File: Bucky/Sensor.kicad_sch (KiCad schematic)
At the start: 4 parts, among them IC2001 INA239AQDGSRQ1

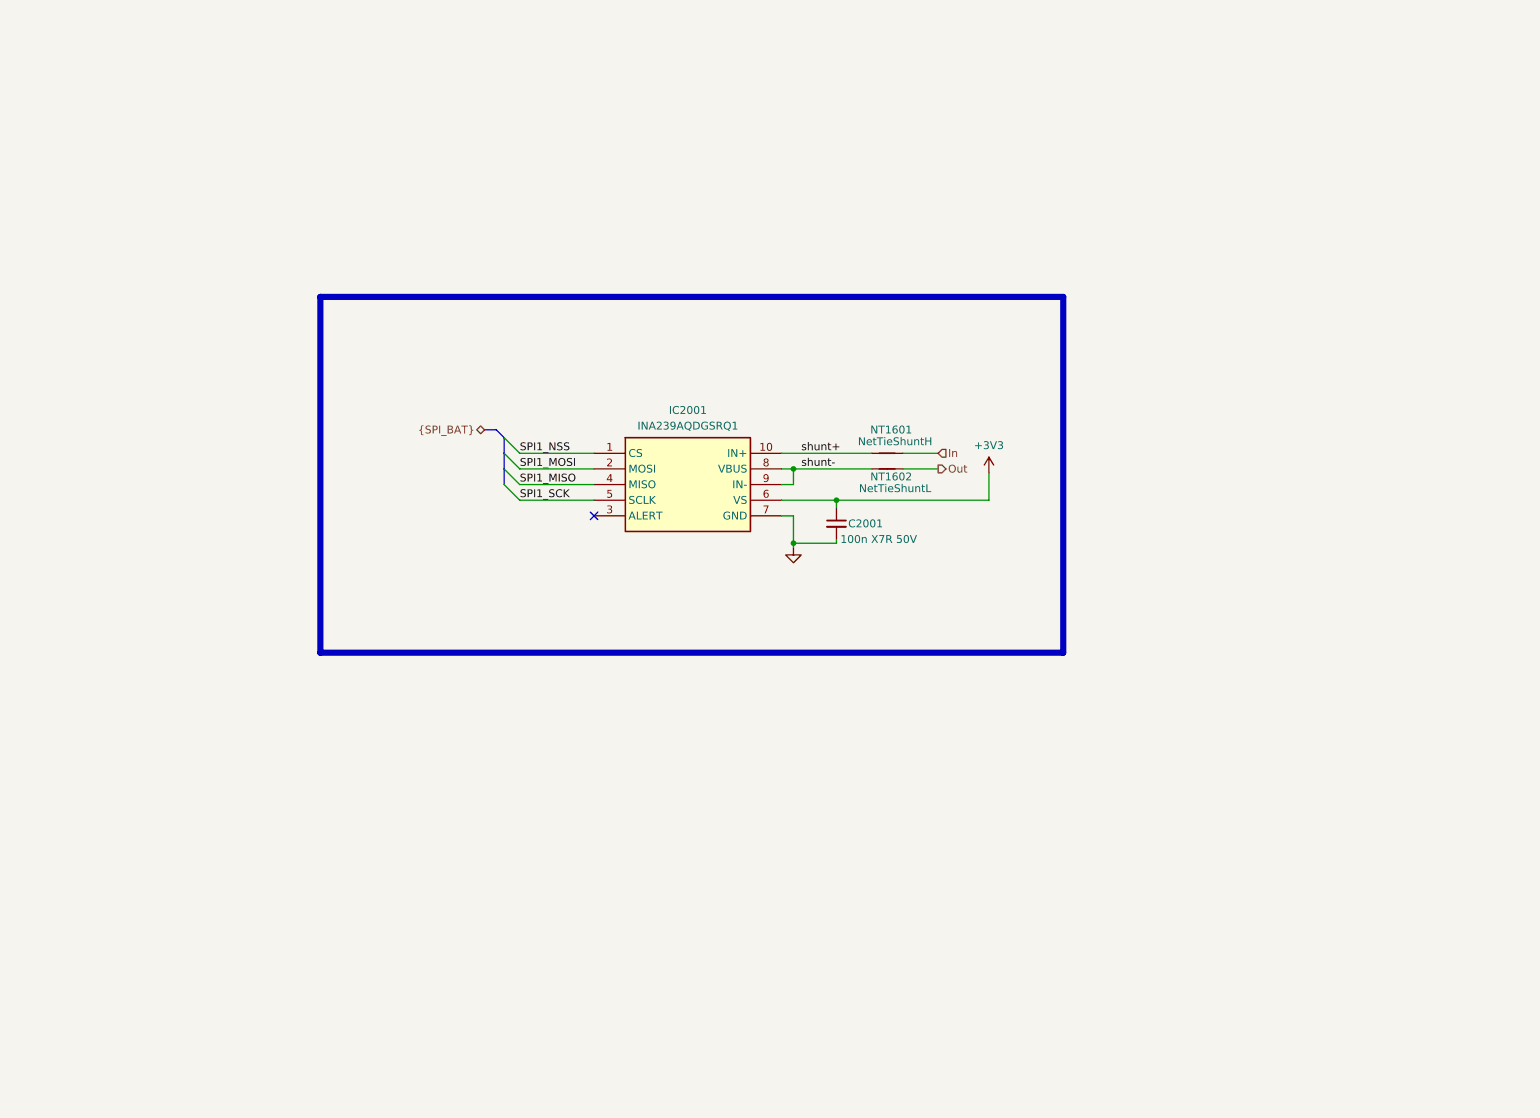
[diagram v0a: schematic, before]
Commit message: adapted schematics and added more protection from GEODE (Reverse Current)
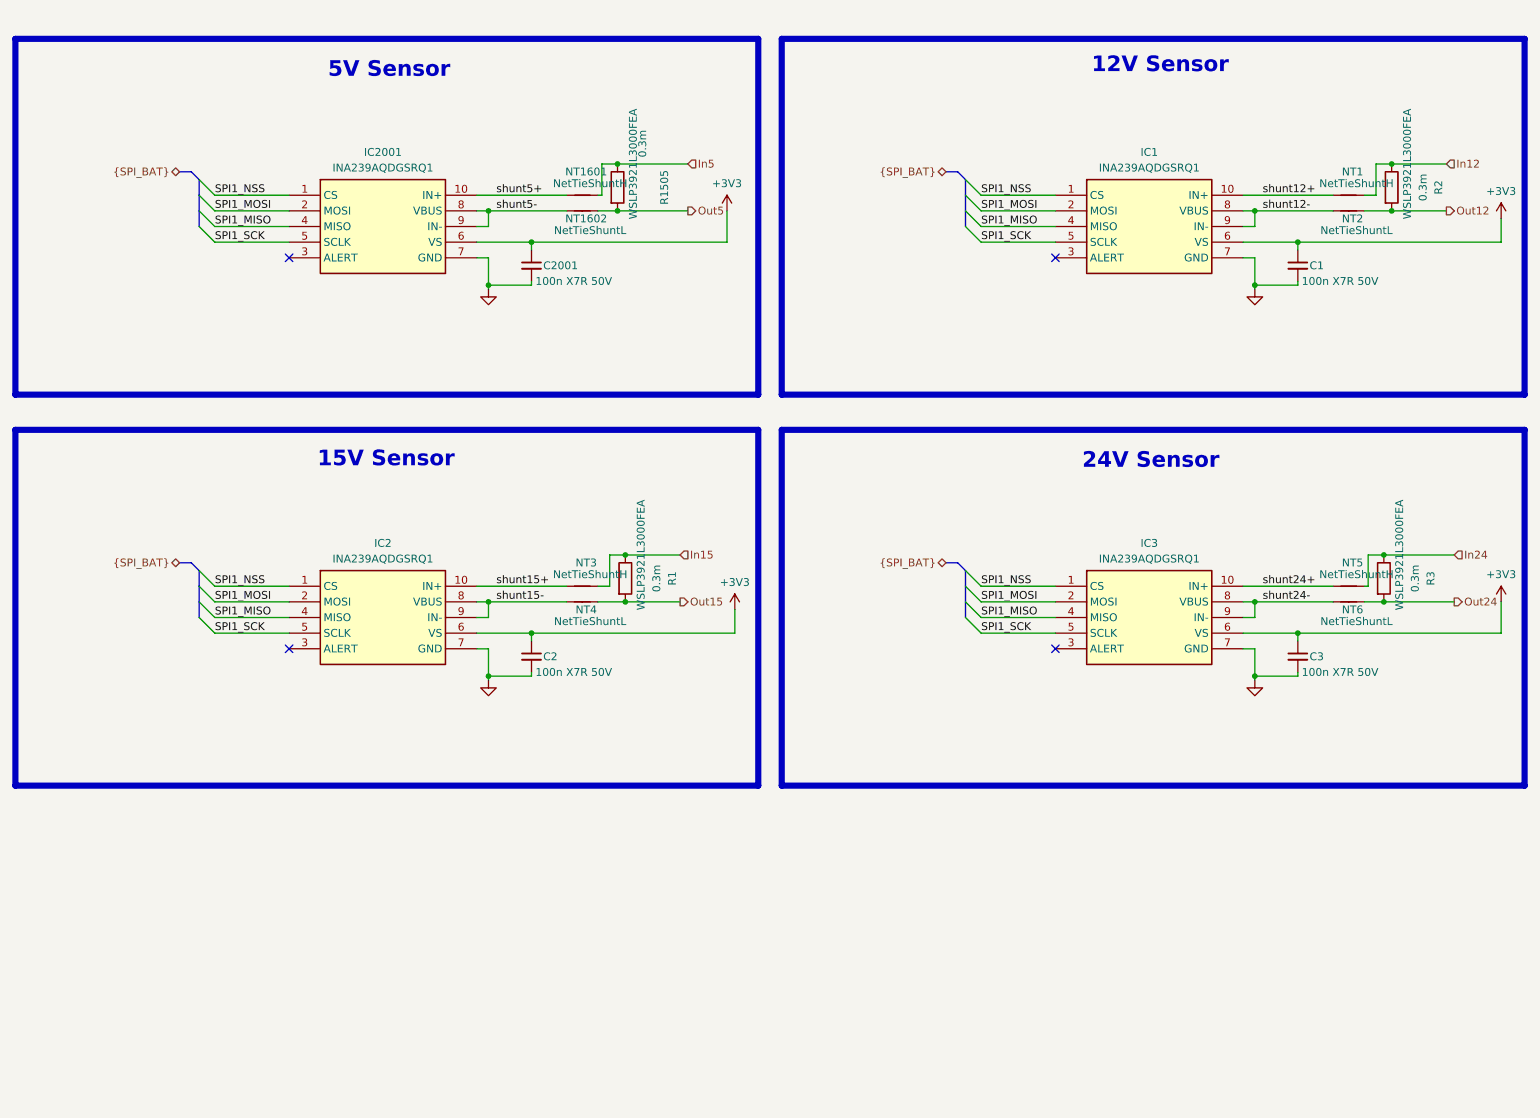
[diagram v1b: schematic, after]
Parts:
- added C1, C2, C3: 100n X7R 50V, 0_capacitor_smd:C_0402_1005_DensityHigh, symbol Device:C_Small
- added IC1, IC2, IC3: INA239AQDGSRQ1, 0_diode_smd:SOP50P490X110-10N, symbol INA239AQDGSRQ1:INA239AQDGSRQ1
- added NT1, NT3, NT5: NetTieShuntH, 0_net_tie:NetTie-2_SMD_Pad0.2mm, symbol Device:NetTie_2
- added NT2, NT4, NT6: NetTieShuntL, 0_net_tie:NetTie-2_SMD_Pad0.2mm, symbol Device:NetTie_2
- added R1, R1505, R2, R3: 0.3m, 0_resistor_smd:RES_WSLP3921_.003OHM_VIS, symbol Device:R
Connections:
- net +3V3: now also C1.1, C2.1, C3.1, IC1.6 (VS), IC2.6 (VS), IC3.6 (VS)
- net GND: now also C1.2, C2.2, C3.2, IC1.7 (GND), IC2.7 (GND), IC3.7 (GND)
- net SPI1_MISO: now also IC1.4 (MISO), IC2.4 (MISO), IC3.4 (MISO)
- net SPI1_MOSI: now also IC1.2 (MOSI), IC2.2 (MOSI), IC3.2 (MOSI)
- net SPI1_NSS: now also IC1.1 (CS), IC2.1 (CS), IC3.1 (CS)
- net SPI1_SCK: now also IC1.5 (SCLK), IC2.5 (SCLK), IC3.5 (SCLK)
- net In renamed In5
- net In5: now also R1505.1
- net Out renamed Out5
- net Out5: now also R1505.2
- net shunt+ renamed shunt5+
- net shunt- renamed shunt5-
- new net In12: NT1.2, R2.1
- new net In15: NT3.2, R1.1
- new net In24: NT5.2, R3.1
- new net Out12: NT2.2, R2.2
- new net Out15: NT4.2, R1.2
- new net Out24: NT6.2, R3.2
- new net shunt12+: IC1.10 (IN+), NT1.1
- new net shunt12-: IC1.8 (VBUS), IC1.9 (IN-), NT2.1
- new net shunt15+: IC2.10 (IN+), NT3.1
- new net shunt15-: IC2.8 (VBUS), IC2.9 (IN-), NT4.1
- new net shunt24+: IC3.10 (IN+), NT5.1
- new net shunt24-: IC3.8 (VBUS), IC3.9 (IN-), NT6.1
- no-connect marks 1 -> 4
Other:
- note added: "12V Sensor"
- note added: "15V Sensor"
- note added: "24V Sensor"
- note added: "5V Sensor"
- moved on the sheet: C2001, IC2001, NT1601, NT1602

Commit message: upadated scchematics
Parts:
- added C8: 100n X7R 50V, 0_capacitor_smd:C_0402_1005_DensityHigh, symbol Device:C_Small
- added IC6: INA239AQDGSRQ1, 0_diode_smd:SOP50P490X110-10N, symbol INA239AQDGSRQ1:INA239AQDGSRQ1
- added NT7: NetTieShuntH, 0_net_tie:NetTie-2_SMD_Pad0.2mm, symbol Device:NetTie_2
- added NT8: NetTieShuntL, 0_net_tie:NetTie-2_SMD_Pad0.2mm, symbol Device:NetTie_2
- added R8: 0.3m, 0_resistor_smd:RES_WSLP3921_.003OHM_VIS, symbol Device:R
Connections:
- net +3V3: now also C8.1, IC6.6 (VS)
- net GND: now also C8.2, IC6.7 (GND)
- net SPI1_MISO: now also IC6.4 (MISO)
- net SPI1_MOSI: now also IC6.2 (MOSI)
- net SPI1_SCK: now also IC6.5 (SCLK)
- removed net SPI1_NSS: IC1.1 (CS), IC2.1 (CS), IC2001.1 (CS), IC3.1 (CS)
- new net InBatt: NT7.2, R8.1
- new net OutBatt: NT8.2, R8.2
- new net SPI1_NSS0: IC2001.1 (CS)
- new net SPI1_NSS1: IC1.1 (CS)
- new net SPI1_NSS2: IC2.1 (CS)
- new net SPI1_NSS3: IC3.1 (CS)
- new net SPI1_NSS4: IC6.1 (CS)
- new net shuntBatt+: IC6.10 (IN+), NT7.1
- new net shuntBatt-: IC6.8 (VBUS), IC6.9 (IN-), NT8.1
- no-connect marks 4 -> 5
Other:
- note added: "Battery Sensor"
- moved on the sheet: C1, C2, C2001, C3, IC1, IC2, IC2001, IC3, NT1, NT1601, NT1602, NT2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
